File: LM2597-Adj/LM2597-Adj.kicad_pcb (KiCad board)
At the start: 2 copper layers, 19.6 x 32.4 mm, 12 parts, among them IC1 LM2597MX-ADJ_NOPB, J1 Conn_01x03

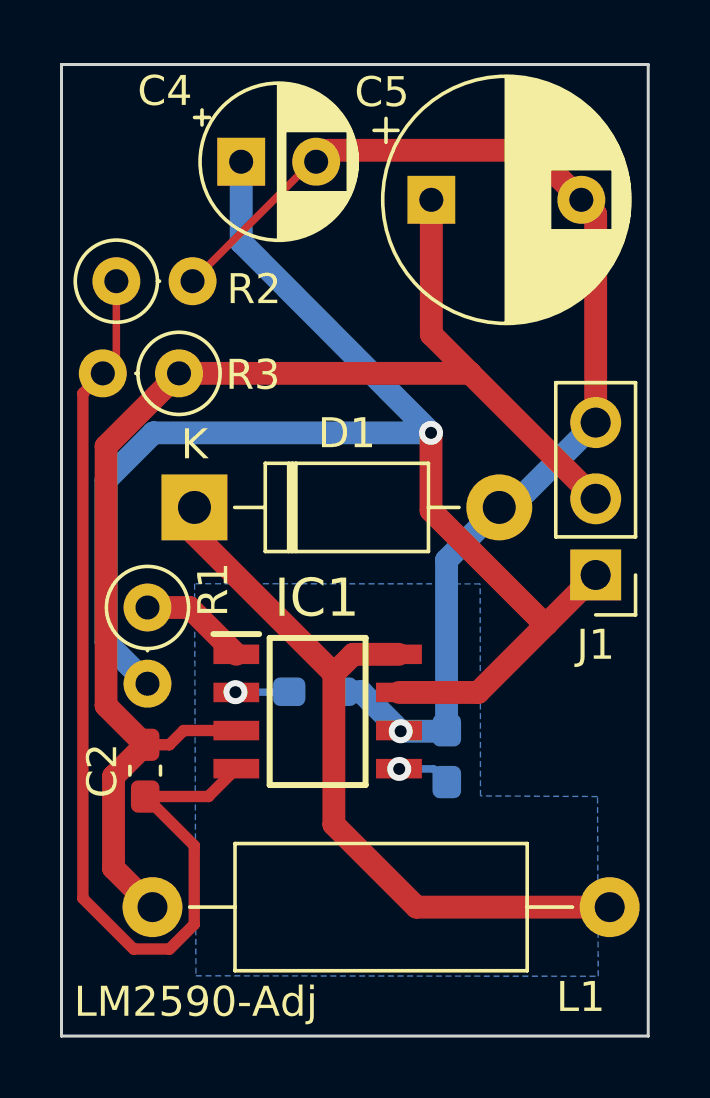
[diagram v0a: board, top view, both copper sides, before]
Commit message: updated all of these to SMD parts
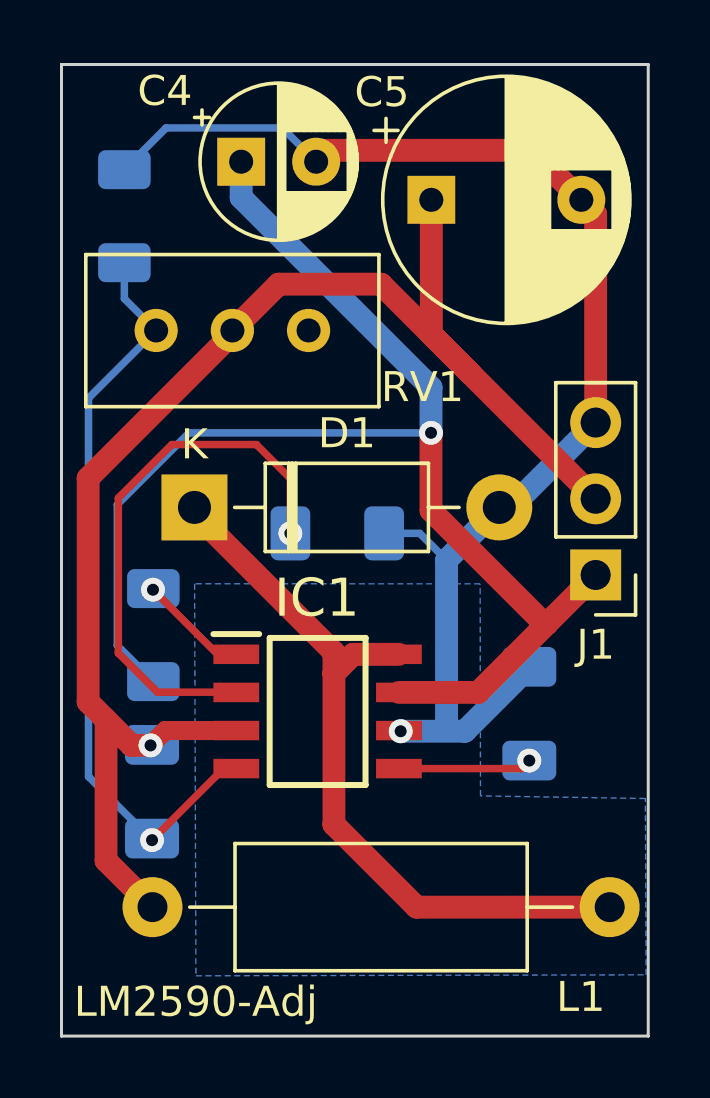
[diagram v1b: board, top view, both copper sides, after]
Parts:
- removed R3: 6.2k, Resistor_THT:R_Axial_DIN0207_L6.3mm_D2.5mm_P2.54mm_Vertical
- added RV1: 200k, Potentiometer_THT:Potentiometer_Bourns_3296W_Vertical, F.Cu at (167.3, 72.2)
- C1, C3: footprint Capacitor_SMD:C_0603_1608Metric_Pad1.08x0.95mm_HandSolder -> Capacitor_SMD:C_1206_3216Metric_Pad1.33x1.80mm_HandSolder
- C2: footprint Capacitor_SMD:C_0603_1608Metric_Pad1.08x0.95mm_HandSolder -> Capacitor_SMD:C_1206_3216Metric_Pad1.33x1.80mm_HandSolder; moved to B.Cu
- R1, R2: footprint Resistor_THT:R_Axial_DIN0207_L6.3mm_D2.5mm_P2.54mm_Vertical -> Resistor_SMD:R_1206_3216Metric_Pad1.30x1.75mm_HandSolder; moved to B.Cu
- moved C1 5.33 mm to (168.2, 79.0)
- moved C3 3.09 mm to (174.6, 85.0)
- moved R2 2.18 mm to (161.1, 68.4), turned to 90 degrees
- moved R1 0.94 mm to (162.1, 82.4)
- moved C2 0.74 mm to (162.1, 87.6)
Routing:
- net Net-(IC1-DELAY): track 1.78 -> 18.4 mm
- net Net-(IC1-FEEDBACK): track 33.5 -> 25.3 mm, vias 0 -> 1
- net GND: track 39.1 -> 44.5 mm
- net VCC: track 45.5 -> 49.0 mm, vias 0 -> 1
- net Net-(IC1-~{SHUTDOWN}/SOFT-START): track 1.77 -> 4.46 mm
- net +VDC: track 46.7 -> 45.7 mm
- net Net-(IC1-ERROR_FLAG): track 3.61 -> 3.67 mm, vias 0 -> 1
